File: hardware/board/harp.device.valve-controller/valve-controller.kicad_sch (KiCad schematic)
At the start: 1 part, among them J26 Conn_02x10_Odd_Even

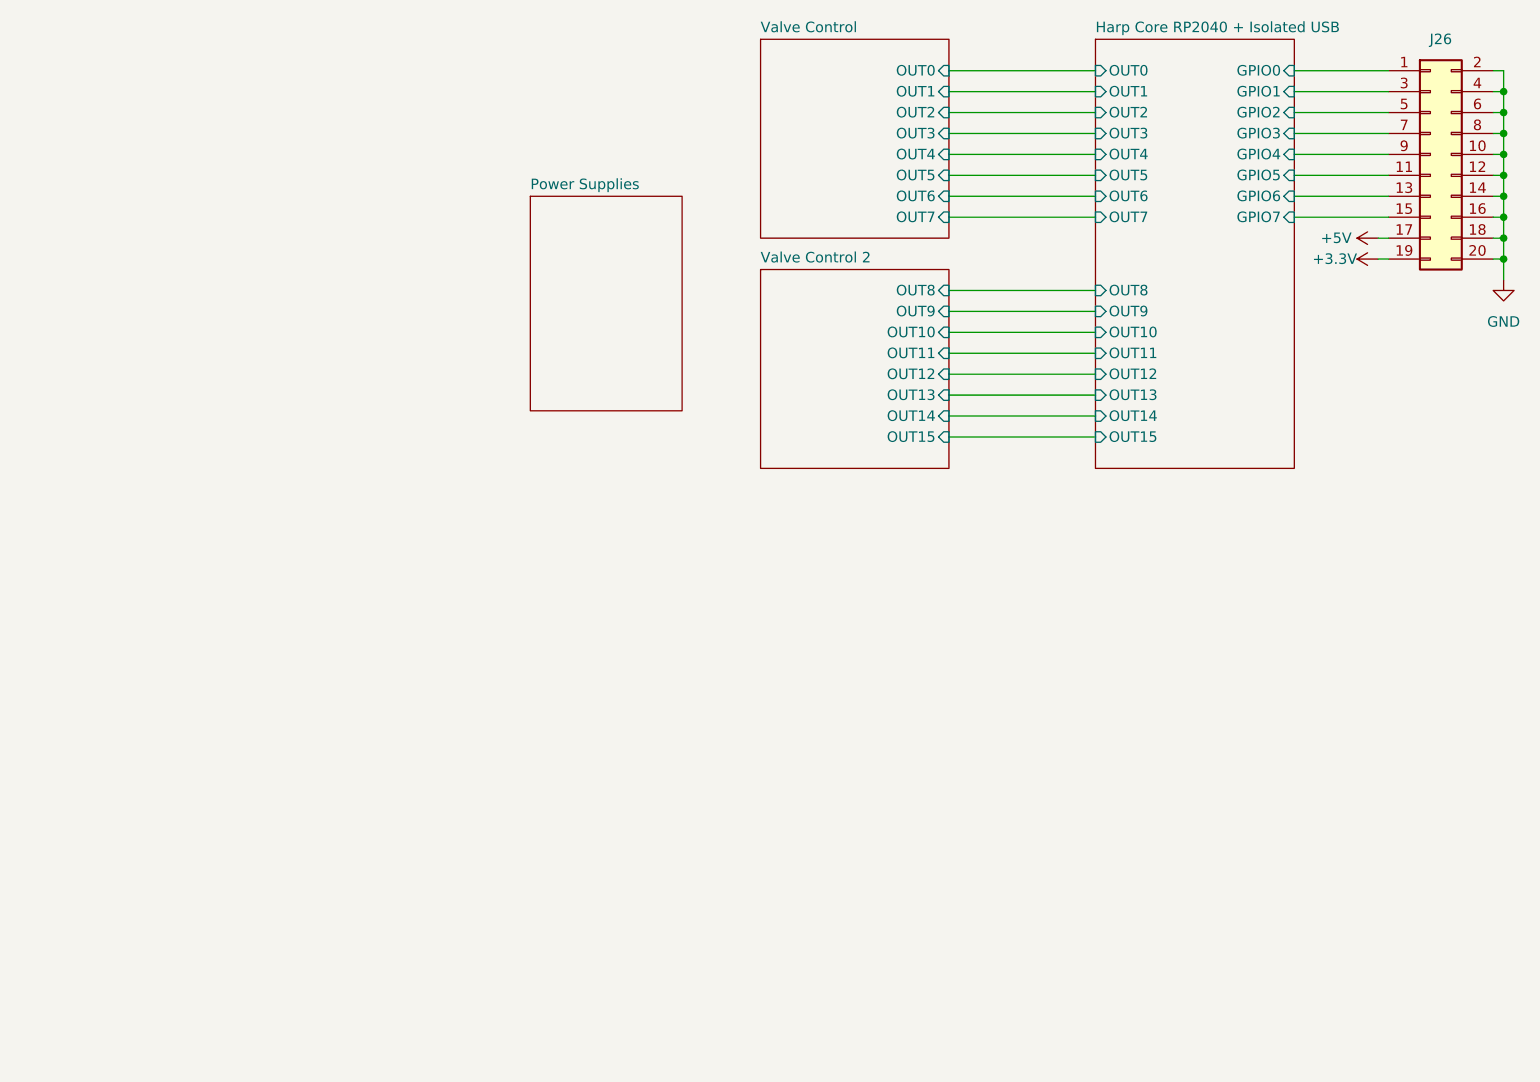
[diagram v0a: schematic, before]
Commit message: add soft start ic; add status LEDs per output
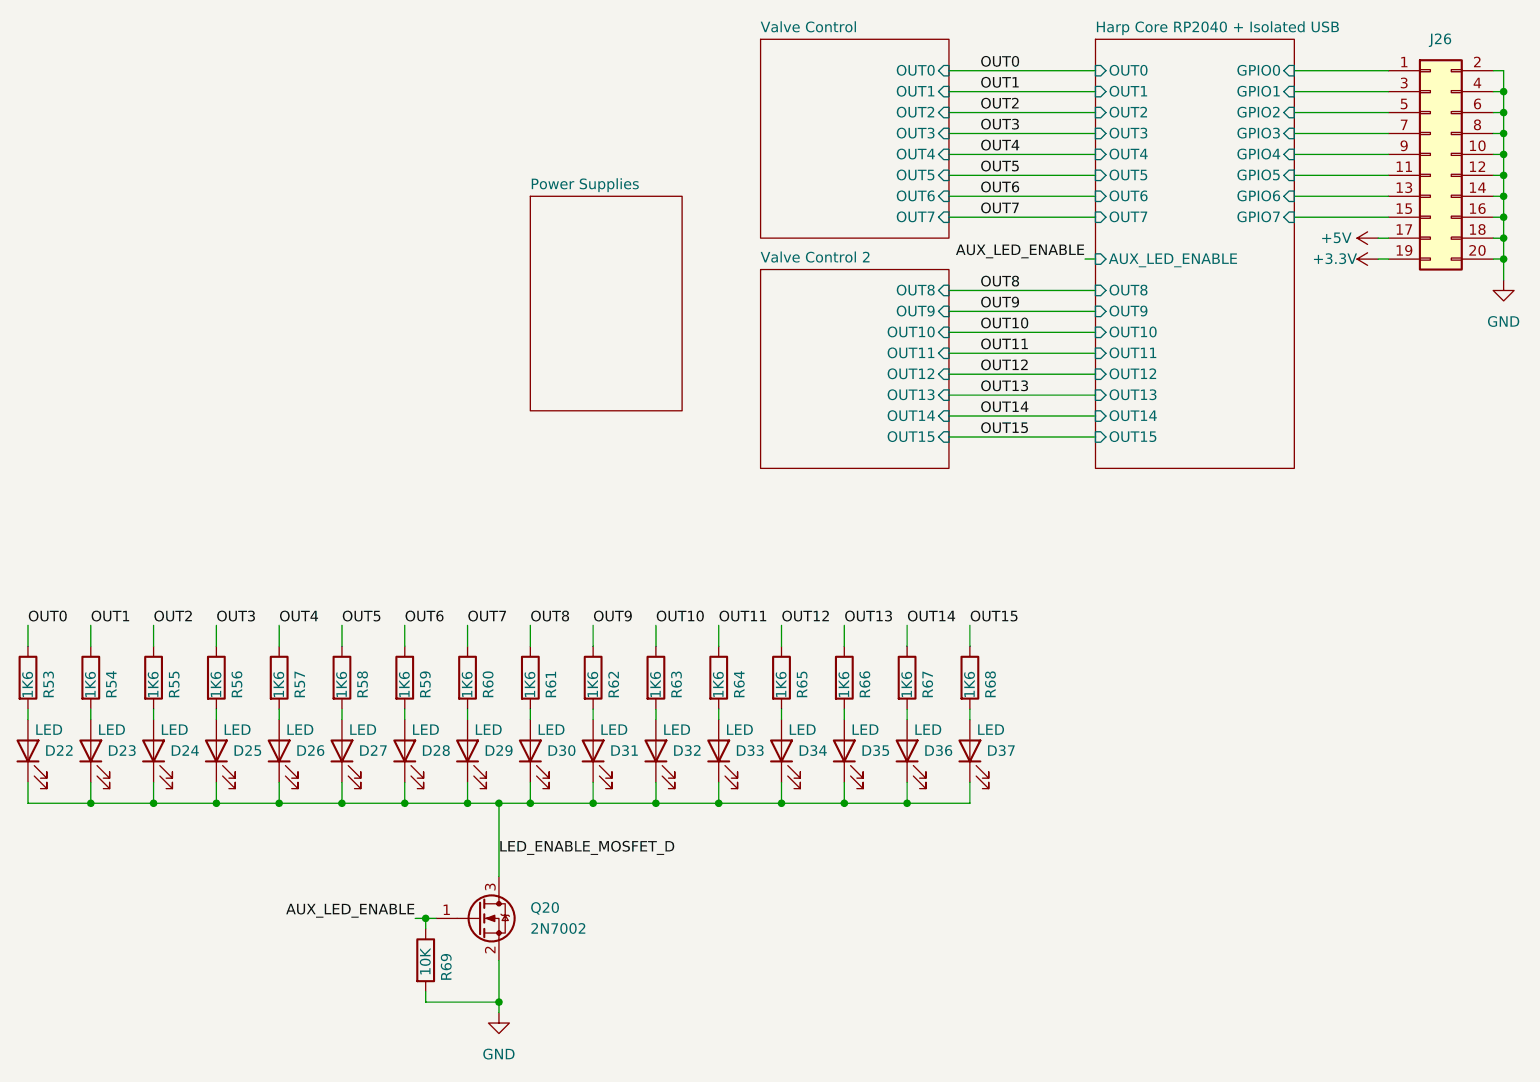
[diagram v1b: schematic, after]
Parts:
- added D22, D23, D24, D25, D26, D27, D28, D29, D30, D31, D32, D33, D34, D35, D36, D37: LED, LED_SMD:LED_0603_1608Metric_Pad1.05x0.95mm_HandSolder, symbol Device:LED
- added Q20: 2N7002, Package_TO_SOT_SMD:SOT-23, symbol Transistor_FET:2N7002
- added R53, R54, R55, R56, R57, R58, R59, R60, R61, R62, R63, R64, R65, R66, R67, R68: 1K6, Resistor_SMD:R_0402_1005Metric, symbol Device:R
- added R69: 10K, Resistor_SMD:R_0402_1005Metric, symbol Device:R
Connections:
- net GND: now also Q20.2 (S), R69.2
- new net: D35.2 (A), R66.2
- new net: D36.2 (A), R67.2
- new net: D31.2 (A), R62.2
- new net: D25.2 (A), R56.2
- new net: D37.2 (A), R68.2
- new net: D34.2 (A), R65.2
- new net: D24.2 (A), R55.2
- new net: D30.2 (A), R61.2
- new net: D22.2 (A), R53.2
- new net: D28.2 (A), R59.2
- new net: D29.2 (A), R60.2
- new net: D27.2 (A), R58.2
- new net: D26.2 (A), R57.2
- new net: D33.2 (A), R64.2
- new net: D23.2 (A), R54.2
- new net: D32.2 (A), R63.2
- new net AUX_LED_ENABLE: Q20.1 (G), R69.1
- new net LED_ENABLE_MOSFET_D: D22.1 (K), D23.1 (K), D24.1 (K), D25.1 (K), D26.1 (K), D27.1 (K), D28.1 (K), D29.1 (K), D30.1 (K), D31.1 (K), D32.1 (K), D33.1 (K), D34.1 (K), D35.1 (K), D36.1 (K), D37.1 (K), Q20.3 (D)
- new net OUT0: R53.1
- new net OUT1: R54.1
- new net OUT10: R63.1
- new net OUT11: R64.1
- new net OUT12: R65.1
- new net OUT13: R66.1
- new net OUT14: R67.1
- new net OUT15: R68.1
- new net OUT2: R55.1
- new net OUT3: R56.1
- new net OUT4: R57.1
- new net OUT5: R58.1
- new net OUT6: R59.1
- new net OUT7: R60.1
- new net OUT8: R61.1
- new net OUT9: R62.1
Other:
- sheet Harp Core RP2040 + Isolated USB ports: added AUX_LED_ENABLE; removed none
